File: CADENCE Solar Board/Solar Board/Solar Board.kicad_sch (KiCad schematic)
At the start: 22 parts, among them U1 INA230AIRGTT, U2 AD7414ARTZ-1REEL7, U3 OPT3001IDNPRQ1

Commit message: Delted unnecessary files, added project files, and custom footprints
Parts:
- removed TP2: Rail Voltage, symbol Connector:TestPoint
- removed TP3: Shunt Voltage, symbol Connector:TestPoint
- removed TP4: SDA, symbol Connector:TestPoint
- removed TP5: SCL, symbol Connector:TestPoint
- removed TP6, TP7: Alert, symbol Connector:TestPoint
- added J1: Conn_01x08, symbol Connector_Generic:Conn_01x08
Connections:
- net +VIN is gone; now on net +3.3V: R4.1, TP1.1, U1.11 (BUS), U1.12 (IN-)
- net +3.3V: now also J1.1 (Pin_1)
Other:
- moved on the sheet: C1

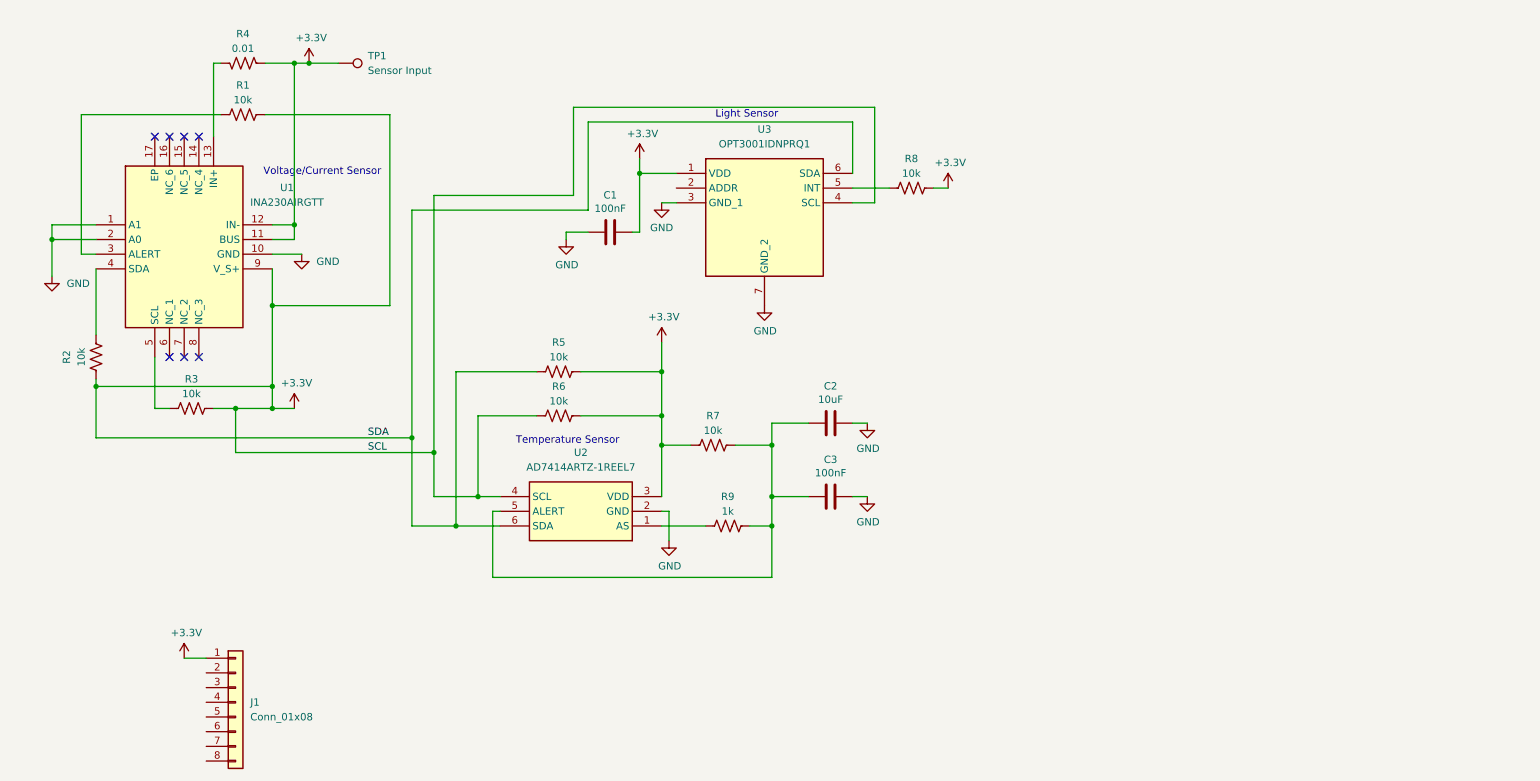
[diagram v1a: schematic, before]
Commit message: Solar board updates - connectros added, schematic simplified with flags, more descriptions, added resistor
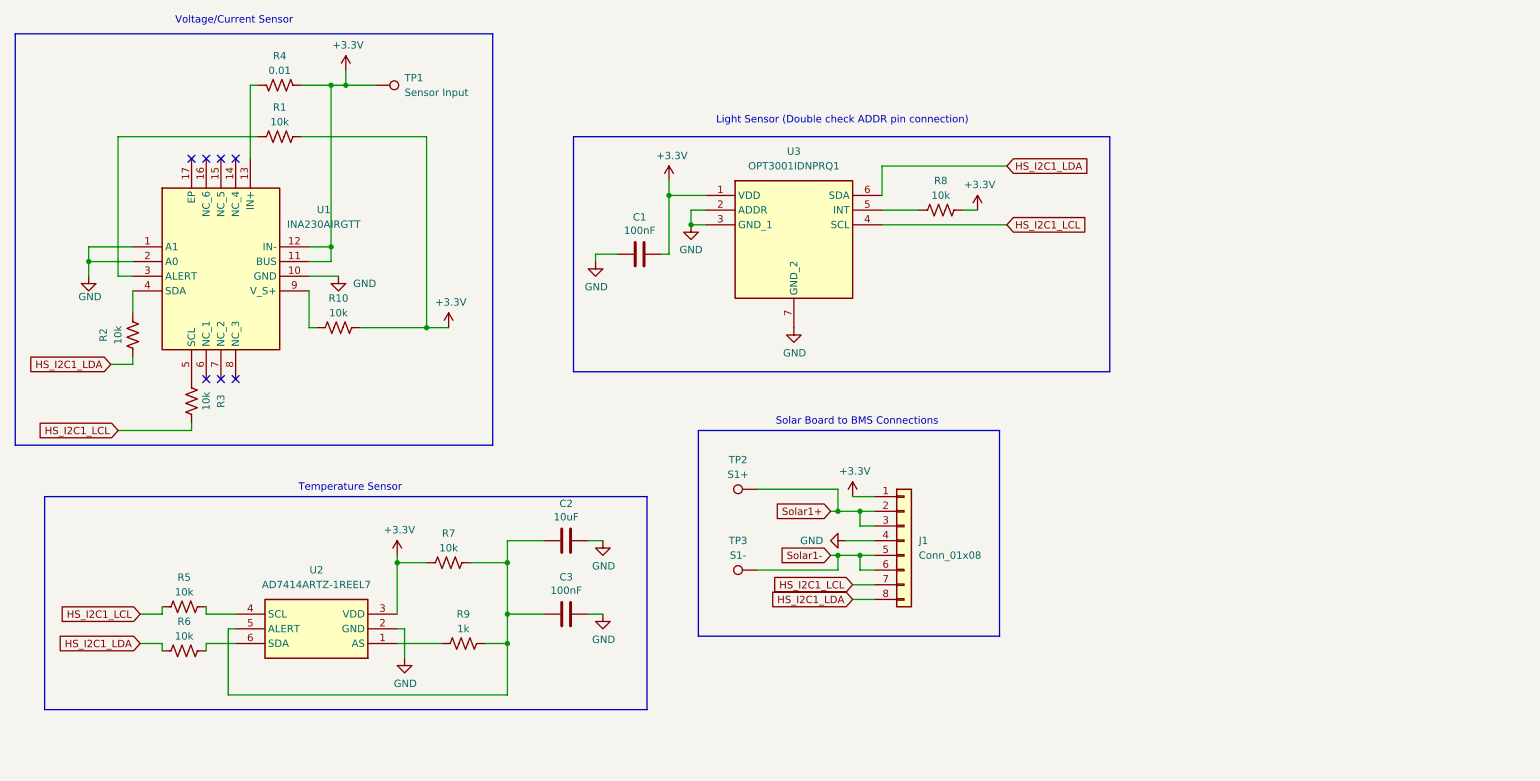
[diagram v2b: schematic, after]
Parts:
- added R10: 10k, symbol Device:R_US
- added TP2: S1+, symbol Connector:TestPoint
- added TP3: S1-, symbol Connector:TestPoint
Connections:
- net +3.3V: now also R10.2; no longer R2.1, R3.2, R5.1, R5.2, R6.1, R6.2, U1.9 (V_S+), U2.4 (SCL), U2.6 (SDA), U3.4 (SCL), U3.6 (SDA)
- net GND: now also J1.4 (Pin_4), U3.2 (ADDR)
- net Solar1+: now reaches J1.2 (Pin_2)
- net Solar1+: now also J1.3 (Pin_3), TP2.1
- net Solar1-: now reaches J1.5 (Pin_5)
- net Solar1-: now also J1.6 (Pin_6), TP3.1
- net HS_I2C1_LCL: now reaches J1.7 (Pin_7)
- net HS_I2C1_LCL: now also R3.2, R5.1, U3.4 (SCL)
- net HS_I2C1_LDA: now reaches J1.8 (Pin_8)
- net HS_I2C1_LDA: now also R2.1, R6.1, U3.6 (SDA)
- new net: R10.1, U1.9 (V_S+)
- new net: R5.2, U2.4 (SCL)
- new net: R6.2, U2.6 (SDA)
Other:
- note added: "Light Sensor (Double check ADDR pin connection)"
- note added: "Solar Board to BMS Connections"
- note removed: "Light Sensor"
- moved on the sheet: C1, C2, C3, J1, R1, R2, R3, R4, R5, R6, R7, R8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

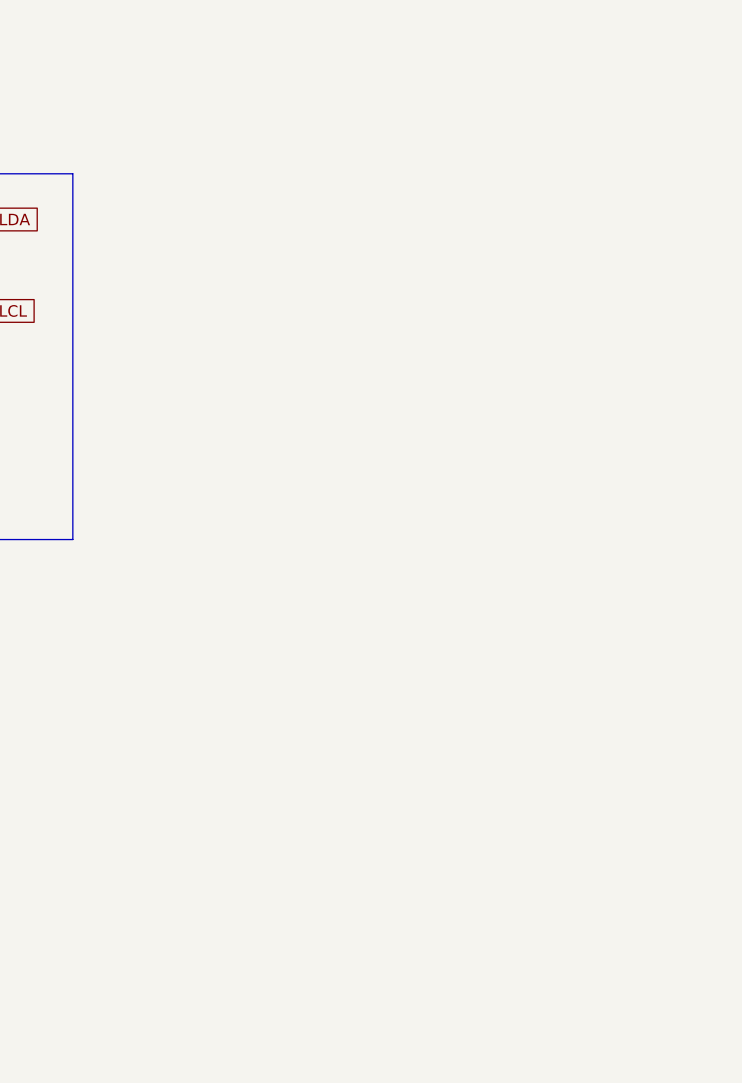
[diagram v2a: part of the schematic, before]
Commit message: added solar cells with diodes
8s2p solar cell configuration with bypass diodes
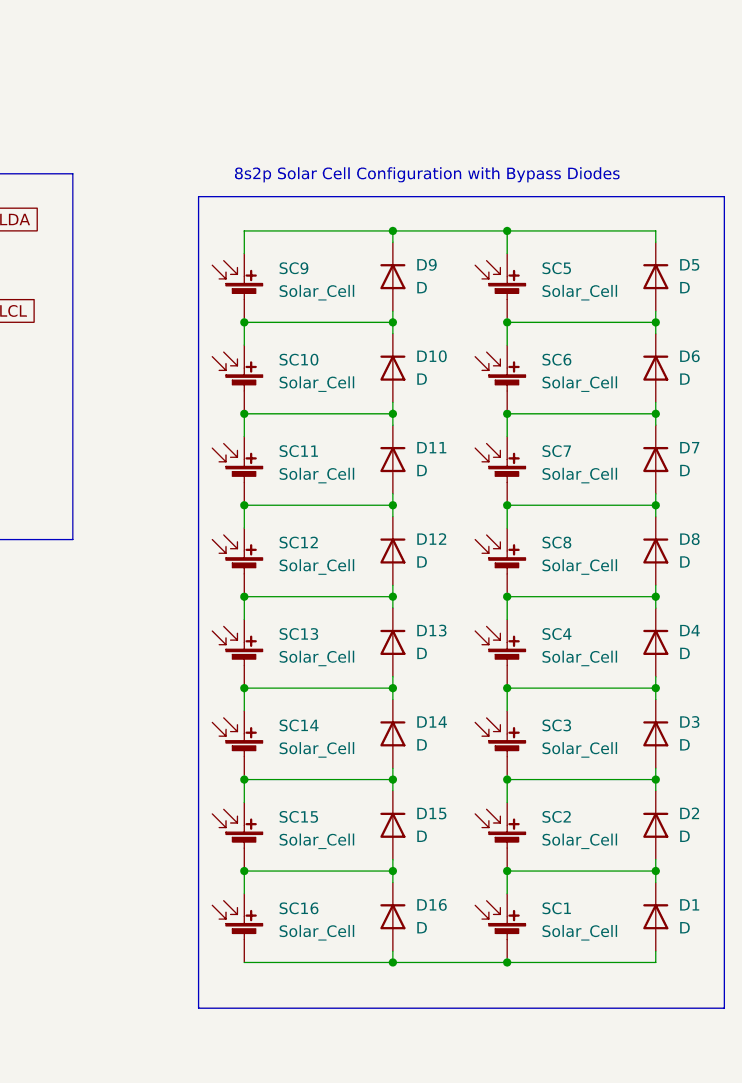
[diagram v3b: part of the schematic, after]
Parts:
- added D1, D10, D11, D12, D13, D14, D15, D16, D2, D3, D4, D5, D6, D7, D8, D9: D, symbol Device:D
- added SC1, SC10, SC11, SC12, SC13, SC14, SC15, SC16, SC2, SC3, SC4, SC5, SC6, SC7, SC8, SC9: Solar_Cell, symbol Device:Solar_Cell
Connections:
- new net: D10.1 (K), D9.2 (A), SC10.1 (+), SC9.2 (-)
- new net: D10.2 (A), D11.1 (K), SC10.2 (-), SC11.1 (+)
- new net: D11.2 (A), D12.1 (K), SC11.2 (-), SC12.1 (+)
- new net: D12.2 (A), D13.1 (K), SC12.2 (-), SC13.1 (+)
- new net: D5.1 (K), D9.1 (K), SC5.1 (+), SC9.1 (+)
- new net: D6.2 (A), D7.1 (K), SC6.2 (-), SC7.1 (+)
- new net: D7.2 (A), D8.1 (K), SC7.2 (-), SC8.1 (+)
- new net: D13.2 (A), D14.1 (K), SC13.2 (-), SC14.1 (+)
- new net: D1.1 (K), D2.2 (A), SC1.1 (+), SC2.2 (-)
- new net: D1.2 (A), D16.2 (A), SC1.2 (-), SC16.2 (-)
- new net: D14.2 (A), D15.1 (K), SC14.2 (-), SC15.1 (+)
- new net: D15.2 (A), D16.1 (K), SC15.2 (-), SC16.1 (+)
- new net: D4.1 (K), D8.2 (A), SC4.1 (+), SC8.2 (-)
- new net: D2.1 (K), D3.2 (A), SC2.1 (+), SC3.2 (-)
- new net: D5.2 (A), D6.1 (K), SC5.2 (-), SC6.1 (+)
- new net: D3.1 (K), D4.2 (A), SC3.1 (+), SC4.2 (-)
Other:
- note added: "8s2p Solar Cell Configuration with Bypass Diodes"
